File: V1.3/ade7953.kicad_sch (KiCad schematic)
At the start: 59 parts, among them U2 ADE7953xCP, Y1 3.58MHz

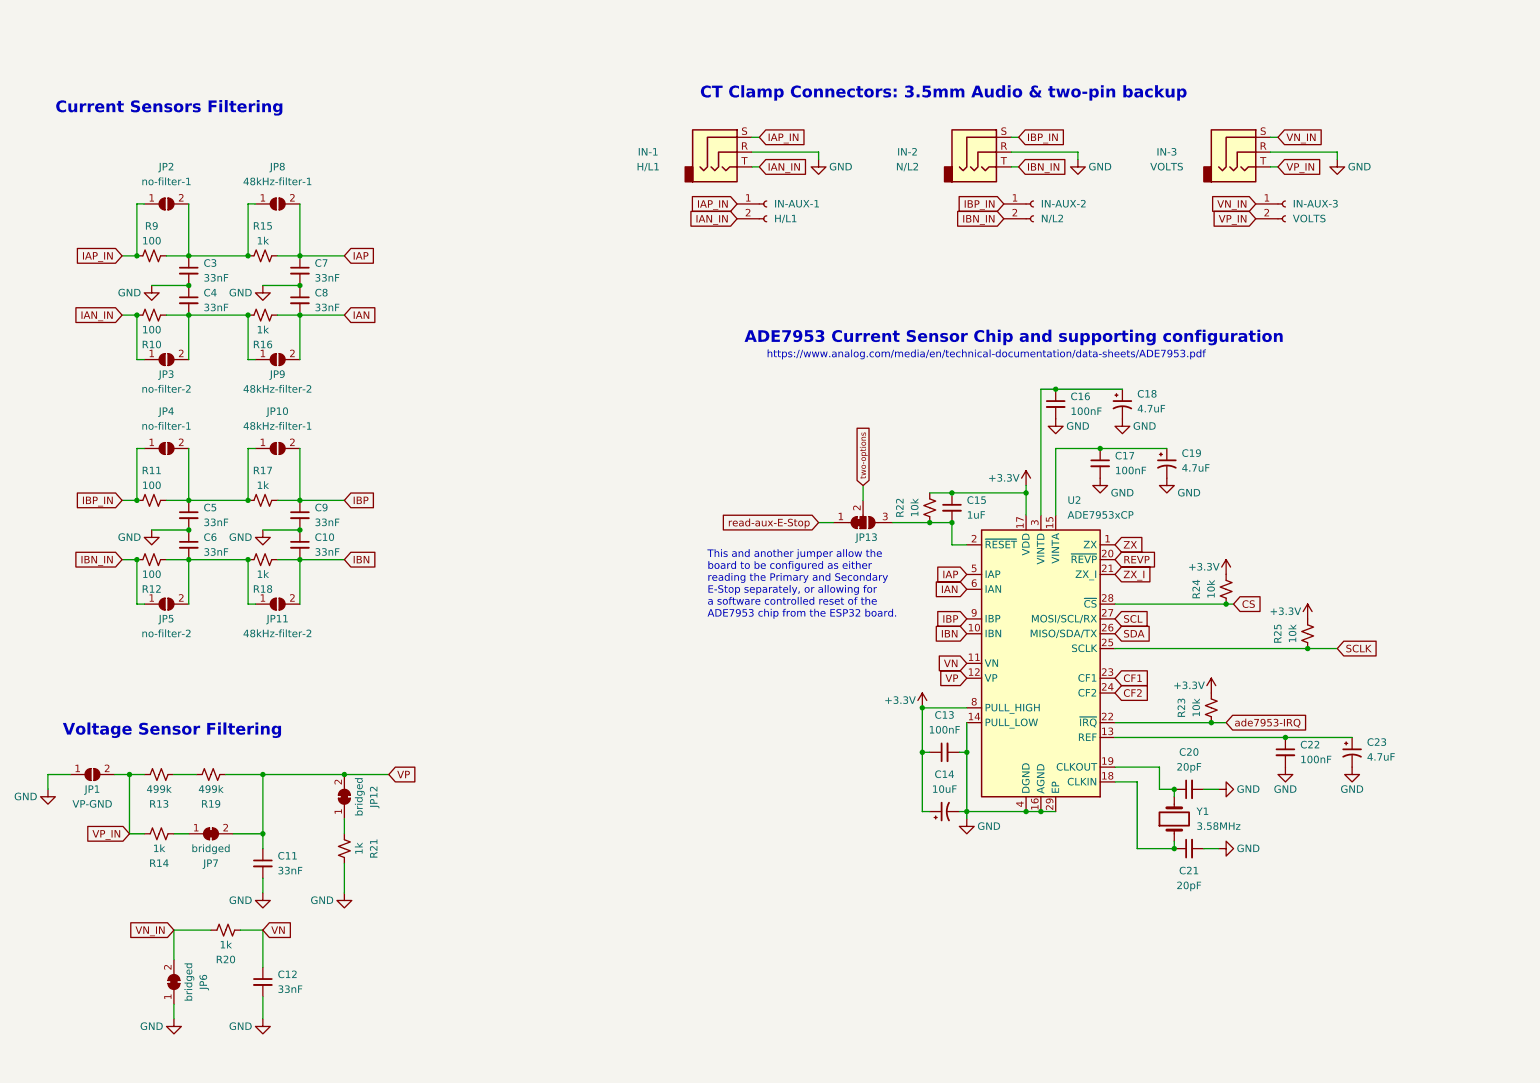
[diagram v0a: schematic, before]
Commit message: rerouted to save space
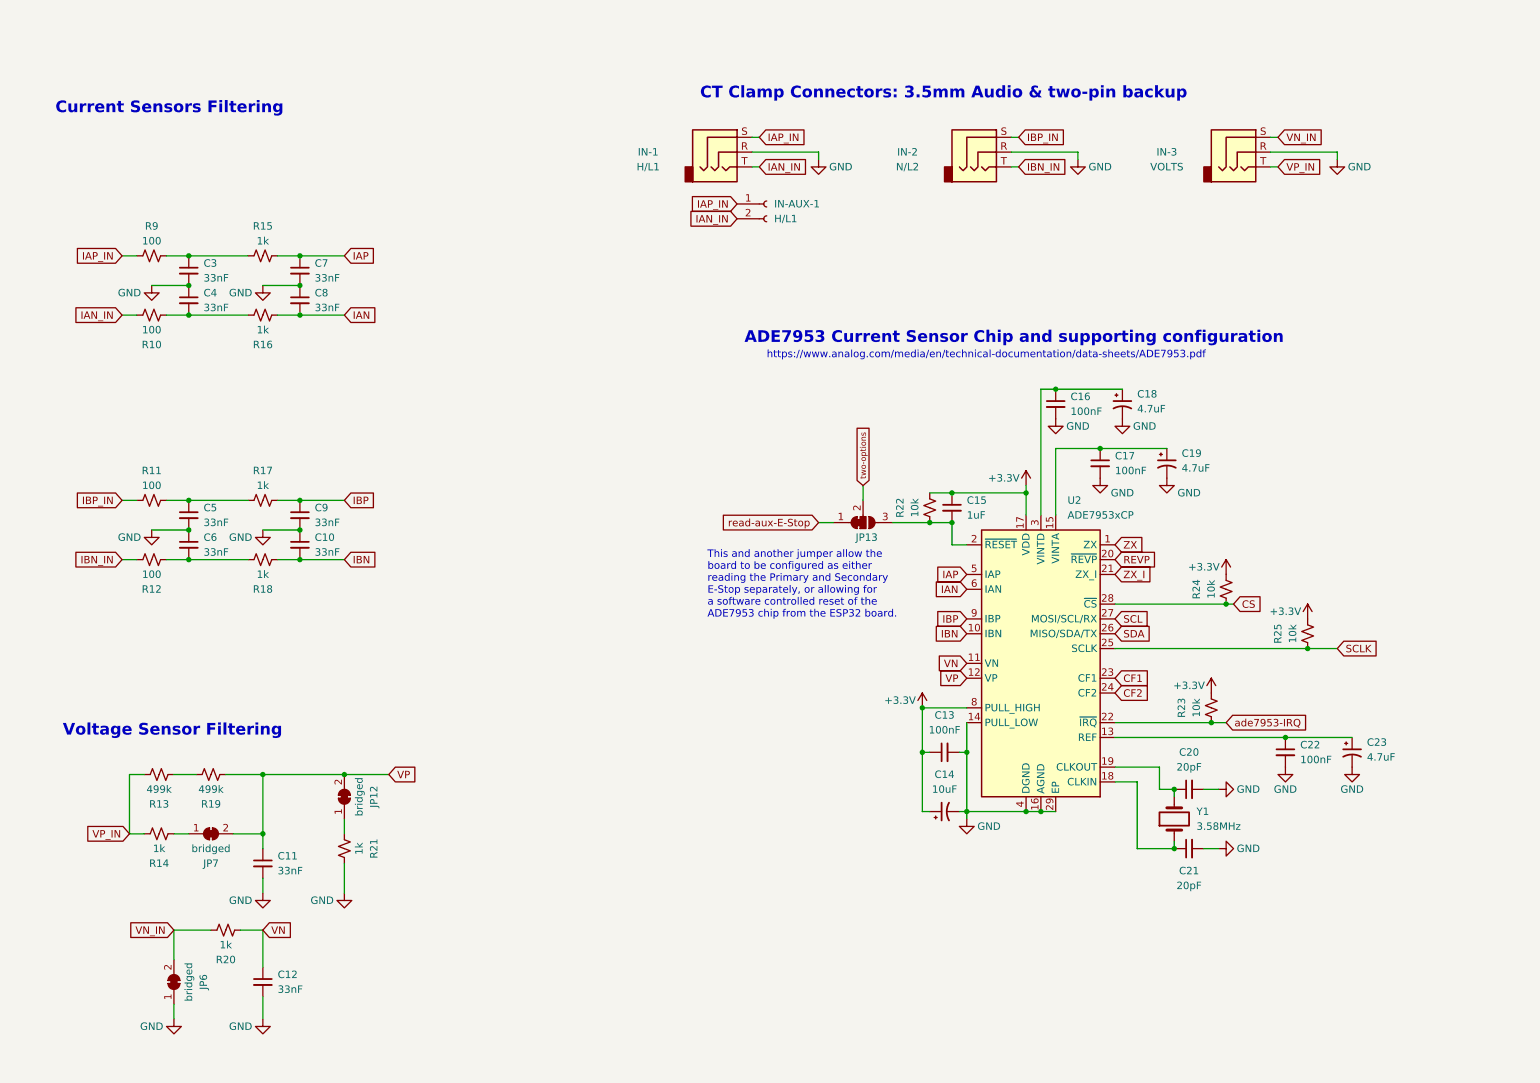
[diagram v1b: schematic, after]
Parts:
- removed IN-AUX-2: N/L2, Connector_PinHeader_2.54mm:PinHeader_1x02_P2.54mm_Vertical, symbol Connector:Conn_01x02_Female
- removed IN-AUX-3: VOLTS, Connector_PinHeader_2.54mm:PinHeader_1x02_P2.54mm_Vertical, symbol Connector:Conn_01x02_Female
- removed JP1: VP-GND, Jumper:SolderJumper-2_P1.3mm_Open_RoundedPad1.0x1.5mm, symbol Jumper:SolderJumper_2_Open
- removed JP10, JP8: 48kHz-filter-1, Jumper:SolderJumper-2_P1.3mm_Open_RoundedPad1.0x1.5mm, symbol Jumper:SolderJumper_2_Open
- removed JP11, JP9: 48kHz-filter-2, Jumper:SolderJumper-2_P1.3mm_Open_RoundedPad1.0x1.5mm, symbol Jumper:SolderJumper_2_Open
- removed JP2, JP4: no-filter-1, Jumper:SolderJumper-2_P1.3mm_Open_RoundedPad1.0x1.5mm, symbol Jumper:SolderJumper_2_Open
- removed JP3, JP5: no-filter-2, Jumper:SolderJumper-2_P1.3mm_Open_RoundedPad1.0x1.5mm, symbol Jumper:SolderJumper_2_Open

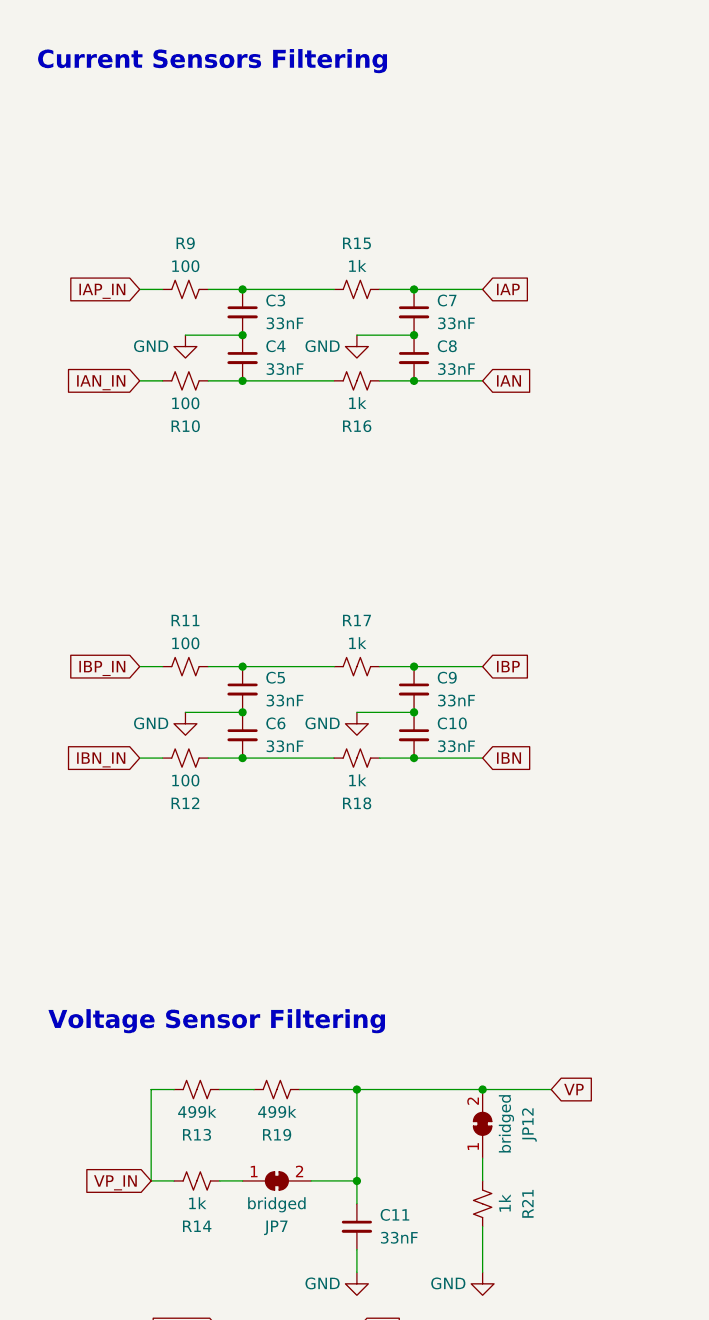
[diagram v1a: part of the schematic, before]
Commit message: jumpers added to bottom
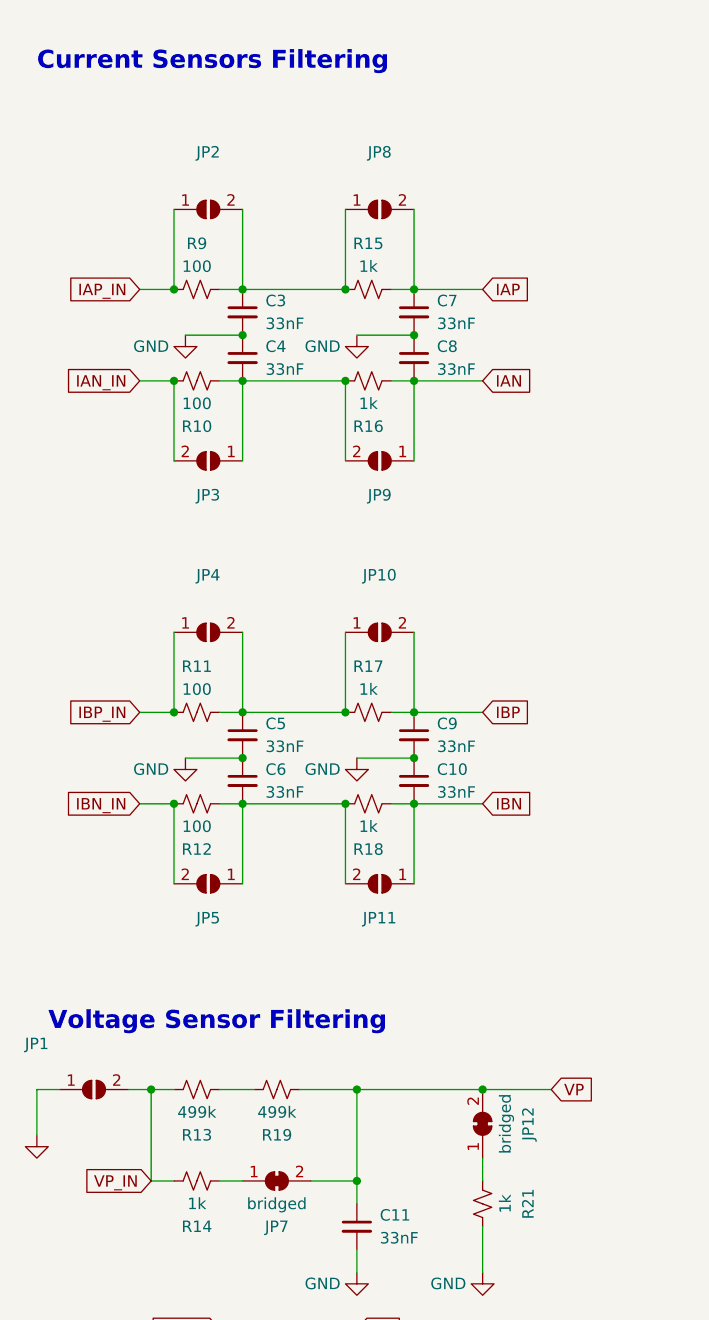
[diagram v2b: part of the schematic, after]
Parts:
- added JP1, JP10, JP11, JP2, JP3, JP4, JP5, JP8, JP9: (no value), symbol Jumper:SolderJumper_2_Open
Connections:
- net GND: now also JP1.1 (A)
- net IAN: now also JP9.1 (A)
- net IAN_IN: now also JP3.2 (B)
- net IAP: now also JP8.2 (B)
- net IAP_IN: now also JP2.1 (A)
- net IBN: now also JP11.1 (A)
- net IBN_IN: now also JP5.2 (B)
- net IBP: now also JP10.2 (B)
- net IBP_IN: now also JP4.1 (A)
- net VP_IN: now also JP1.2 (B)
- net at C5.1, R11.2, R17.1: now also JP10.1 (A), JP4.2 (B)
- net at C6.2, R12.1, R18.2: now also JP11.2 (B), JP5.1 (A)
- net at C4.2, R10.1, R16.2: now also JP3.1 (A), JP9.2 (B)
- net at C3.1, R15.1, R9.2: now also JP2.2 (B), JP8.1 (A)
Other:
- moved on the sheet: C10, C5, C6, C9, R10, R11, R12, R15, R16, R17, R18, R9

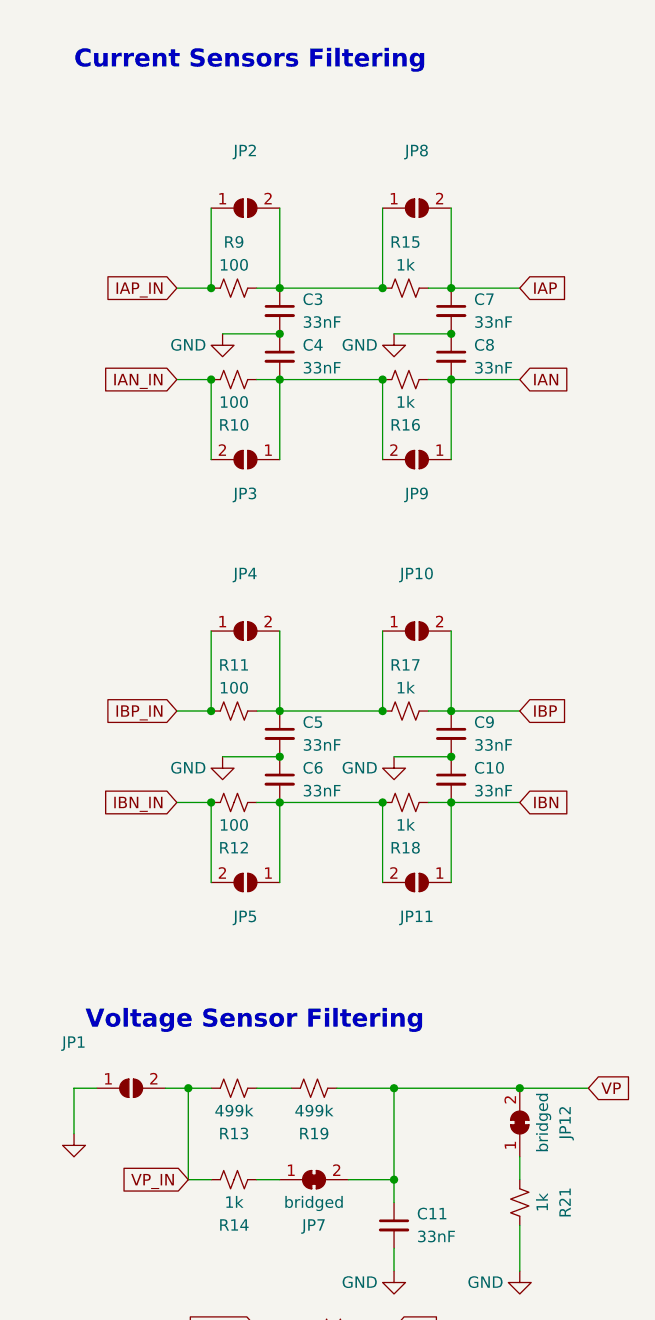
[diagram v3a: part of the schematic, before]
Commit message: close the last ratsnests
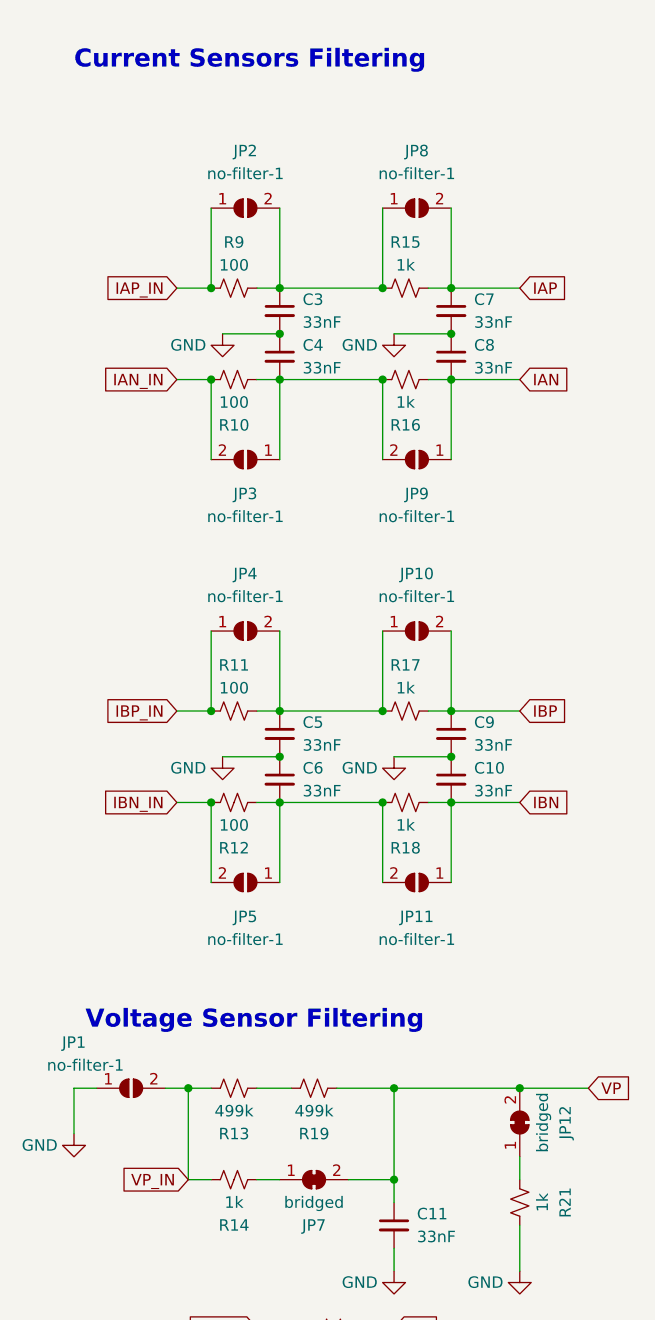
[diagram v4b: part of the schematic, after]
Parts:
- JP1, JP10, JP11, JP2, JP3, JP4, JP5, JP8, JP9: value (none) -> no-filter-1; footprint (none) -> Jumper:SolderJumper-2_P1.3mm_Open_RoundedPad1.0x1.5mm
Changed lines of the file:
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@@
     (in_bom yes) (on_board yes) (fields_autoplaced)
     (property "Reference" "JP2" (id 0) (at 44.45 40.64 0))
-    (property "Value" "" (id 1) (at 44.45 43.18 0))
-    (property "Footprint" "" (id 2) (at 44.45 46.99 0)
+    (property "Value" "no-filter-1" (id 1) (at 44.45 43.18 0))
+    (property "Footprint" "Jumper:SolderJumper-2_P1.3mm_Open_RoundedPad1.0x1.5mm" (id 2) (at 44.45 46.99 0)
       (effects (font (size 1.27 1.27)) hide)
     )
@@
     (in_bom yes) (on_board yes) (fields_autoplaced)
     (property "Reference" "JP8" (id 0) (at 63.5 40.64 0))
-    (property "Value" "" (id 1) (at 63.5 43.18 0))
-    (property "Footprint" "" (id 2) (at 63.5 46.99 0)
+    (property "Value" "no-filter-1" (id 1) (at 63.5 43.18 0))
+    (property "Footprint" "Jumper:SolderJumper-2_P1.3mm_Open_RoundedPad1.0x1.5mm" (id 2) (at 63.5 46.99 0)
       (effects (font (size 1.27 1.27)) hide)
     )
@@
       (effects (font (size 1.27 1.27)) hide)
     )
-    (property "Value" "" (id 1) (at 21.59 151.13 0))
+    (property "Value" "GND" (id 1) (at 21.59 151.13 0))
     (property "Footprint" "" (id 2) (at 25.4 149.86 0)
       (effects (font (size 1.27 1.27)) hide)
@@
     (in_bom yes) (on_board yes)
     (property "Reference" "JP1" (id 0) (at 25.4 139.7 0))
-    (property "Value" "" (id 1) (at 26.67 142.24 0))
-    (property "Footprint" "" (id 2) (at 31.75 144.78 0)
+    (property "Value" "no-filter-1" (id 1) (at 26.67 142.24 0))
+    (property "Footprint" "Jumper:SolderJumper-2_P1.3mm_Open_RoundedPad1.0x1.5mm" (id 2) (at 31.75 144.78 0)
       (effects (font (size 1.27 1.27)) hide)
     )
@@
     (in_bom yes) (on_board yes)
     (property "Reference" "JP9" (id 0) (at 63.5 78.74 0))
-    (property "Value" "" (id 1) (at 63.5 81.28 0))
-    (property "Footprint" "" (id 2) (at 63.5 74.93 0)
+    (property "Value" "no-filter-1" (id 1) (at 63.5 81.28 0))
+    (property "Footprint" "Jumper:SolderJumper-2_P1.3mm_Open_RoundedPad1.0x1.5mm" (id 2) (at 63.5 74.93 0)
       (effects (font (size 1.27 1.27)) hide)
     )
@@
     (in_bom yes) (on_board yes) (fields_autoplaced)
     (property "Reference" "JP10" (id 0) (at 63.5 87.63 0))
-    (property "Value" "" (id 1) (at 63.5 90.17 0))
-    (property "Footprint" "" (id 2) (at 63.5 93.98 0)
+    (property "Value" "no-filter-1" (id 1) (at 63.5 90.17 0))
+    (property "Footprint" "Jumper:SolderJumper-2_P1.3mm_Open_RoundedPad1.0x1.5mm" (id 2) (at 63.5 93.98 0)
       (effects (font (size 1.27 1.27)) hide)
     )
@@
     (in_bom yes) (on_board yes)
     (property "Reference" "JP3" (id 0) (at 44.45 78.74 0))
-    (property "Value" "" (id 1) (at 44.45 81.28 0))
-    (property "Footprint" "" (id 2) (at 44.45 74.93 0)
+    (property "Value" "no-filter-1" (id 1) (at 44.45 81.28 0))
+    (property "Footprint" "Jumper:SolderJumper-2_P1.3mm_Open_RoundedPad1.0x1.5mm" (id 2) (at 44.45 74.93 0)
       (effects (font (size 1.27 1.27)) hide)
     )
@@
     (in_bom yes) (on_board yes)
     (property "Reference" "JP5" (id 0) (at 44.45 125.73 0))
-    (property "Value" "" (id 1) (at 44.45 128.27 0))
-    (property "Footprint" "" (id 2) (at 44.45 121.92 0)
+    (property "Value" "no-filter-1" (id 1) (at 44.45 128.27 0))
+    (property "Footprint" "Jumper:SolderJumper-2_P1.3mm_Open_RoundedPad1.0x1.5mm" (id 2) (at 44.45 121.92 0)
       (effects (font (size 1.27 1.27)) hide)
     )
@@
     (in_bom yes) (on_board yes)
     (property "Reference" "JP11" (id 0) (at 63.5 125.73 0))
-    (property "Value" "" (id 1) (at 63.5 128.27 0))
-    (property "Footprint" "" (id 2) (at 63.5 121.92 0)
+    (property "Value" "no-filter-1" (id 1) (at 63.5 128.27 0))
+    (property "Footprint" "Jumper:SolderJumper-2_P1.3mm_Open_RoundedPad1.0x1.5mm" (id 2) (at 63.5 121.92 0)
       (effects (font (size 1.27 1.27)) hide)
     )
@@
     (in_bom yes) (on_board yes) (fields_autoplaced)
     (property "Reference" "JP4" (id 0) (at 44.45 87.63 0))
-    (property "Value" "" (id 1) (at 44.45 90.17 0))
-    (property "Footprint" "" (id 2) (at 44.45 93.98 0)
-      (effects (font (size 1.27 1.27)) hide)
-    )
+    (property "Value" "no-filter-1" (id 1) (at 44.45 90.17 0))
+    (property "Footprint" "Jumper:SolderJumper-2_P1.3mm_Open_RoundedPad1.0x1.5mm" (id 2) (at 44.45 93.98 0)
+      (effects (font (size 1.27 1.27)) hide)
+    )

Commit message: update v1.3 schematic documentation
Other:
- note added: "ADE7953 Current Sensor"
- note added: "This current sensor was selected because it was known to work with the ESP32 and ESPHome (the main platforms of this project at large. It took several test-boards to get to a useful integration, yet much of this still just follows the documentation linked above. There are jumpers that can be soldered over, if the circuit needs any kind of fine turing from later observations."
- note removed: "ADE7953 Current Sensor Chip and supporting configuration"
- moved on the sheet: C10, C11, C12, C3, C4, C5, C6, C7, C8, C9, IN-1, IN-2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
